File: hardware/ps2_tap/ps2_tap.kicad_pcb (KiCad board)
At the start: 2 copper layers, 41.1 x 19.2 mm, 7 parts, among them J1 MINI_DIN_6, J2 MINI_DIN_6, J3 JACK_NO_SWITCH

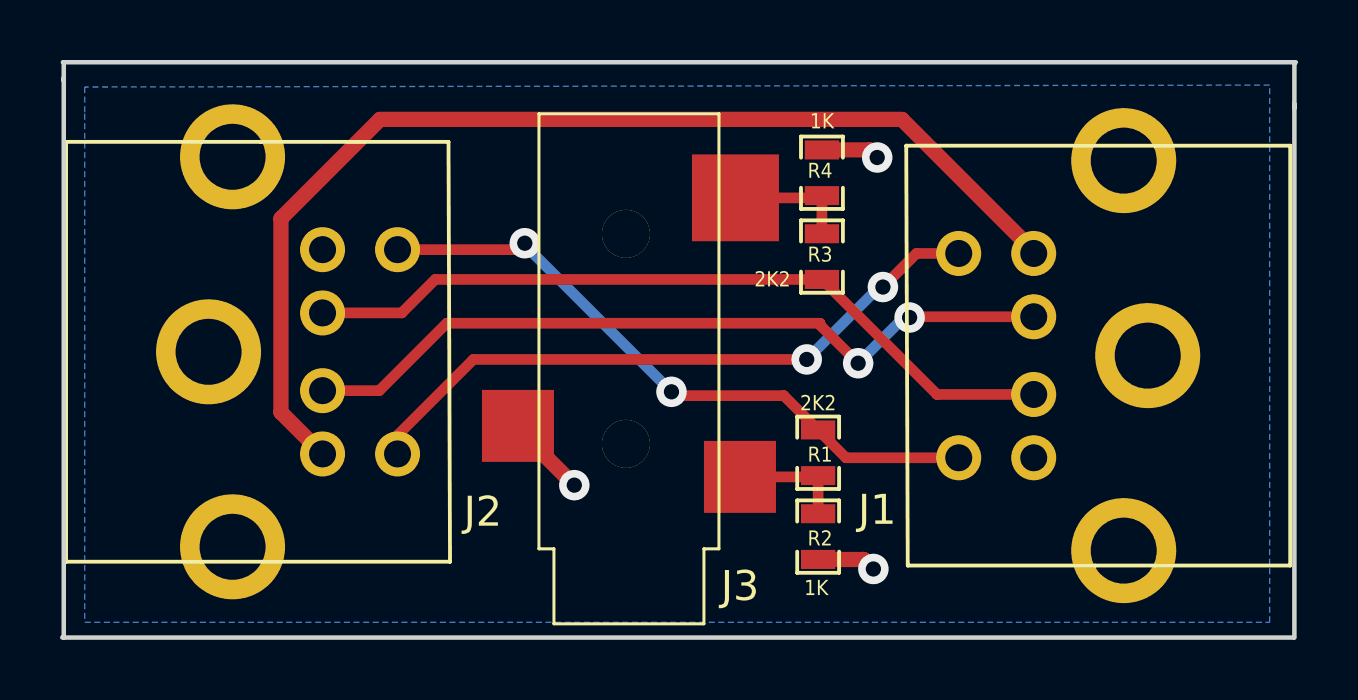
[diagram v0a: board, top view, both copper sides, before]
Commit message: Fix swapped 3.5mm jack pads
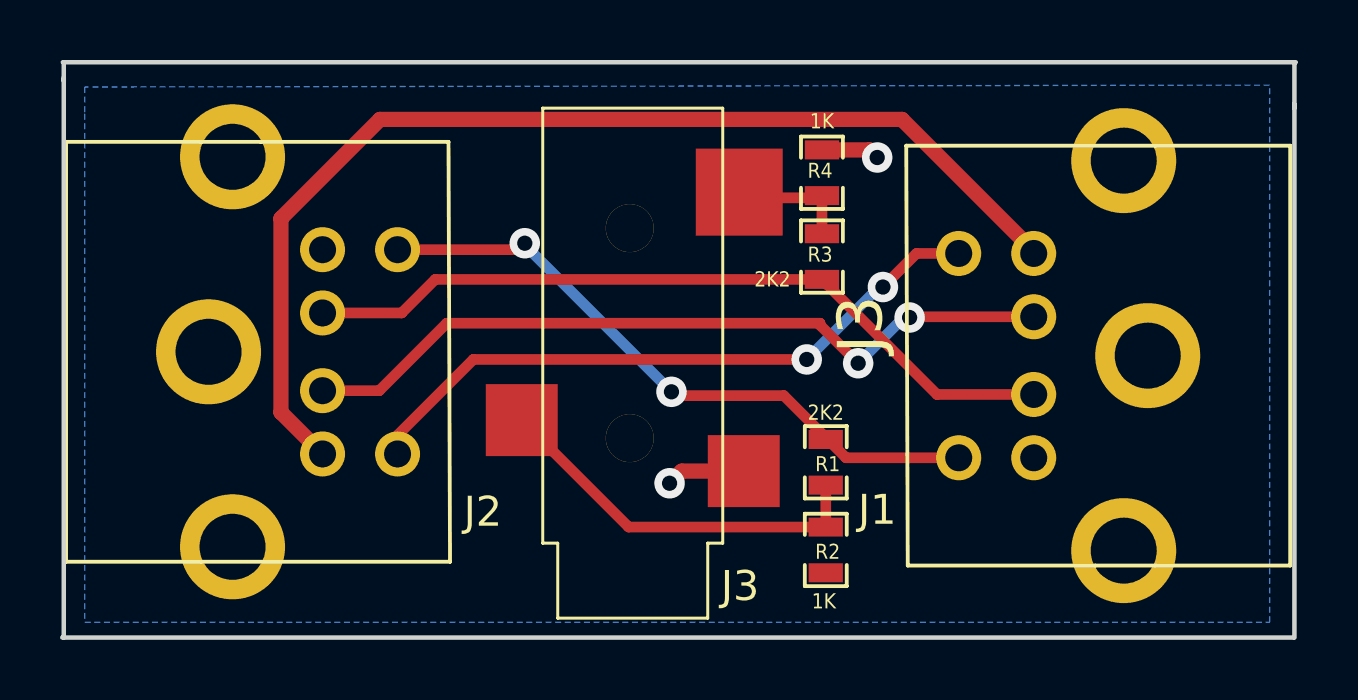
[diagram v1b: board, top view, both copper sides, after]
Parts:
- moved R2 0.51 mm to (205.2, 133.6)
- moved R1 0.41 mm to (205.2, 130.7)
- moved J3 0.23 mm to (198.6, 126.0)
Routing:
- net /CLK_OUT: track 3.81 -> 13.4 mm
- net GND: track 7.03 -> 4.59 mm, vias 3 -> 2
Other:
- board text added: "@dominicgs Rev: 2013-06-12"
- board text removed: "Rev: 2013-05-16"
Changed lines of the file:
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@@
   (general
     (links 15)
-    (no_connects 0)
-    (area 179.590699 114.282334 260.323 174.028)
+    (no_connects 1)
+    (area 179.706199 117.272999 220.975001 136.600001)
     (thickness 1.6)
     (drawings 12)
-    (tracks 58)
+    (tracks 55)
     (zones 0)
     (modules 7)
@@
     (mod_text_size 1.5 1.5)
     (mod_text_width 0.15)
-    (pad_size 1.4 1.4)
-    (pad_drill 0.6)
+    (pad_size 2.4 2.4)
+    (pad_drill 0)
     (pad_to_mask_clearance 0.2)
     (aux_axis_origin 0 0)
@@
       (usegerberextensions true)
       (excludeedgelayer true)
-      (linewidth 152400)
+      (linewidth 0.150000)
       (plotframeref false)
       (viasonmask false)
@@
   )
   (module SM0603_Resistor (layer F.Cu)
-    (at 204.978 130.3655 270)
+    (at 205.232 130.683 270)
     (attr smd)
     (fp_text reference R1 (at 0.0635 -0.0635 360) (layer F.SilkS)
@@
   )
   (module SM0603_Resistor (layer F.Cu)
-    (at 204.978 133.1595 270)
+    (at 205.232 133.604 270)
     (attr smd)
     (fp_text reference R2 (at 0.0635 -0.0635 360) (layer F.SilkS)
@@
   )
   (module JACK_35MM_NO_SWITCH (layer F.Cu)
-    (at 198.501 126.238 90)
-    (fp_text reference J3 (at -0.04 7.77 90) (layer F.SilkS) hide
+    (at 198.628 126.0475 90)
+    (fp_text reference J3 (at -0.04 7.77 90) (layer F.SilkS)
       (effects (font (size 1.5 1.5) (thickness 0.15)))
     )
@@
     (fp_line (start -9.83 2.67) (end -7.33 2.67) (layer F.SilkS) (width 0.1))
     (fp_line (start -9.83 2.67) (end -9.83 -2.33) (layer F.SilkS) (width 0.1))
-    (pad 1 smd rect (at -3.23 -3.53 90) (size 2.4 2.4)
+    (pad 3 smd rect (at -3.23 -3.53 90) (size 2.4 2.4)
+      (layers F.Cu F.Paste F.Mask)
+      (net 2 /CLK_OUT)
+    )
+    (pad 2 smd rect (at 4.37 3.72 90) (size 2.9 2.9)
+      (layers F.Cu F.Paste F.Mask)
+      (net 4 /DATA_OUT)
+    )
+    (pad 1 smd rect (at -4.93 3.87 90) (size 2.4 2.4)
       (layers F.Cu F.Paste F.Mask)
       (net 8 GND)
-    )
-    (pad 2 smd rect (at 4.37 3.72 90) (size 2.9 2.9)
-      (layers F.Cu F.Paste F.Mask)
-      (net 4 /DATA_OUT)
-    )
-    (pad 3 smd rect (at -4.93 3.87 90) (size 2.4 2.4)
-      (layers F.Cu F.Paste F.Mask)
-      (net 2 /CLK_OUT)
     )
     (pad "" thru_hole circle (at -3.83 0.07 90) (size 1.6 1.6) (drill 1.6)
@@
     (effects (font (size 1 1) (thickness 0.1)) (justify mirror))
   )
-  (gr_text "Rev: 2013-05-16" (at 197.0405 125.984 180) (layer B.SilkS)
-    (effects (font (size 1 1) (thickness 0.2)) (justify mirror))
+  (gr_text "@dominicgs\nRev: 2013-06-12" (at 190.754 127.1905 180) (layer B.SilkS)
+    (effects (font (size 1 1) (thickness 0.2)) (justify left mirror))
   )
   (gr_text "Dominic Spill\n<dominicgs@gmail.com>" (at 188.849 134.5565 180) (layer B.SilkS)
@@
   (segment (start 209.6635 130.532) (end 205.9065 130.532) (width 0.3556) (layer F.Cu) (net 1) (status 10))
   (segment (start 205.9065 130.532) (end 204.978 129.6035) (width 0.3556) (layer F.Cu) (net 1) (status 20))
-  (segment (start 202.371 131.168) (end 204.9375 131.168) (width 0.3556) (layer F.Cu) (net 2) (status 30))
-  (segment (start 204.9375 131.168) (end 204.978 131.2085) (width 0.3556) (layer F.Cu) (net 2) (status 30))
-  (segment (start 204.978 131.2085) (end 204.978 132.3975) (width 0.3556) (layer F.Cu) (net 2) (status 30))
+  (segment (start 205.232 132.842) (end 205.232 131.445) (width 0.3556) (layer F.Cu) (net 2) (status 30))
+  (segment (start 205.232 132.842) (end 198.6625 132.842) (width 0.3556) (layer F.Cu) (net 2) (status 10))
+  (segment (start 198.6625 132.842) (end 195.098 129.2775) (width 0.3556) (layer F.Cu) (net 2) (status 20))
+  (segment (start 194.971 129.341) (end 194.971 129.693) (width 0.3556) (layer F.Cu) (net 2) (status 30))
   (segment (start 205.105 124.587) (end 192.2145 124.587) (width 0.3556) (layer F.Cu) (net 3) (status 10))
   (segment (start 192.2145 124.587) (end 191.0965 125.705) (width 0.3556) (layer F.Cu) (net 3))
@@
   (segment (start 187.071 122.555) (end 187.071 129.018) (width 0.508) (layer F.Cu) (net 7))
   (segment (start 188.458 130.405) (end 187.071 129.018) (width 0.508) (layer F.Cu) (net 7) (status 10))
-  (segment (start 204.978 133.9215) (end 206.502 133.9215) (width 0.508) (layer F.Cu) (net 8) (status 10))
-  (segment (start 206.502 133.9215) (end 206.8195 134.239) (width 0.508) (layer F.Cu) (net 8))
-  (via (at 206.8195 134.239) (size 1.016) (layers F.Cu B.Cu) (net 8))
+  (segment (start 202.498 130.9775) (end 200.429 130.9775) (width 0.508) (layer F.Cu) (net 8) (status 10))
+  (via (at 200.025 131.3815) (size 1.016) (layers F.Cu B.Cu) (net 8))
+  (segment (start 200.429 130.9775) (end 200.025 131.3815) (width 0.508) (layer F.Cu) (net 8))
   (segment (start 205.105 120.269) (end 206.6925 120.269) (width 0.508) (layer F.Cu) (net 8) (status 10))
   (segment (start 206.6925 120.269) (end 206.9465 120.523) (width 0.508) (layer F.Cu) (net 8))
   (via (at 206.9465 120.523) (size 1.016) (layers F.Cu B.Cu) (net 8))
-  (segment (start 194.971 129.468) (end 194.971 129.566) (width 0.508) (layer F.Cu) (net 8) (status 30))
-  (segment (start 194.971 129.566) (end 196.85 131.445) (width 0.508) (layer F.Cu) (net 8) (status 10))
-  (via (at 196.85 131.445) (size 1.016) (layers F.Cu B.Cu) (net 8))
-  (segment (start 194.971 129.341) (end 194.971 129.693) (width 0.3556) (layer F.Cu) (net 8) (status 30))
   (zone (net 8) (net_name GND) (layer B.Cu) (hatch edge 0.508)
     (connect_pads (clearance 0.3048))
